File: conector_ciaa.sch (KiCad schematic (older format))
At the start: 2 parts

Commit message: Primer version
Esquematico completo, faltan notas del revisor.
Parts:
- removed J? (x2): CONN_02X20, symbol CONN_02X20
- added XA1: Conn_Poncho2P_2x_20x2, footprints:Conn_Poncho_Completo, symbol Conn_Poncho2P_2x_20x2
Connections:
- net labels added: +3.3V, +5V, ADC_1, GND, GPIO_0, GPIO_1, GPIO_2, GPIO_3, SPI_MISO, SPI_SCK
- wire segments 0 -> 36
- no-connect marks 0 -> 50

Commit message: Primer revision
Se agregar correcciones del revisor. Se modifica entrada termocupla.
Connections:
- net GNDA: now reaches XA1.10 (GNDA)
- no-connect marks 50 -> 49
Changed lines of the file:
@@
 EESchema Schematic File Version 2
-LIBS:tempRalayPoncho-rescue
-LIBS:power
-LIBS:device
-LIBS:transistors
-LIBS:conn
-LIBS:linear
-LIBS:regul
-LIBS:74xx
-LIBS:cmos4000
-LIBS:adc-dac
-LIBS:memory
-LIBS:xilinx
-LIBS:microcontrollers
-LIBS:dsp
-LIBS:microchip
-LIBS:analog_switches
-LIBS:motorola
-LIBS:texas
-LIBS:intel
-LIBS:audio
-LIBS:interface
-LIBS:digital-audio
-LIBS:philips
-LIBS:display
-LIBS:cypress
-LIBS:siliconi
-LIBS:opto
-LIBS:atmel
-LIBS:contrib
-LIBS:valves
-LIBS:ej2cese
-LIBS:analog-cache
-LIBS:ciaa-nxp-cache
-LIBS:relay
-LIBS:cmos_ieee
-LIBS:tempRalayPoncho-cache
+LIBS:TempRelay
+LIBS:tempRelayPoncho-cache
 EELAYER 25 0
 EELAYER END
@@
 Connection ~ 4900 4100
 NoConn ~ 4600 2400
-NoConn ~ 4600 2600
 NoConn ~ 4600 2700
 NoConn ~ 4600 2800
@@
 Wire Wire Line
 	6600 3400 6900 3400
-Wire Wire Line
-	6600 3500 6900 3500
-Connection ~ 6600 3400
 Connection ~ 6600 3100
 Wire Wire Line
 	6600 4000 6900 4000
-Connection ~ 6600 3500
 Wire Wire Line
 	6600 4100 6900 4100
-Connection ~ 6600 4000
 Wire Wire Line
 	6600 4000 6600 4400
@@
 NoConn ~ 8100 4100
 $Comp
-L GND #PWR01
+L GND #PWR3
 U 1 1 594EB190
 P 4900 4400
-F 0 "#PWR01" H 4900 4150 50  0001 C CNN
+F 0 "#PWR3" H 4900 4150 50  0001 C CNN
 F 1 "GND" H 4900 4250 50  0000 C CNN
 F 2 "" H 4900 4400 50  0001 C CNN
@@
 $EndComp
 $Comp
-L GND #PWR02
+L GND #PWR5
 U 1 1 594EB307
 P 6600 4400
-F 0 "#PWR02" H 6600 4150 50  0001 C CNN
+F 0 "#PWR5" H 6600 4150 50  0001 C CNN
 F 1 "GND" H 6600 4250 50  0000 C CNN
 F 2 "" H 6600 4400 50  0001 C CNN
@@
 $EndComp
 $Comp
-L GND #PWR03
+L GND #PWR4
 U 1 1 594EB35A
 P 6200 2600
-F 0 "#PWR03" H 6200 2350 50  0001 C CNN
+F 0 "#PWR4" H 6200 2350 50  0001 C CNN
 F 1 "GND" H 6200 2450 50  0000 C CNN
 F 2 "" H 6200 2600 50  0001 C CNN
@@
 P 3100 2000
 AR Path="/594EB36B" Ref="#PWR5"  Part="1"
-AR Path="/59498167/594EB36B" Ref="#PWR04"  Part="1"
-F 0 "#PWR04" H 3100 1850 50  0001 C CNN
+AR Path="/59498167/594EB36B" Ref="#PWR1"  Part="1"
+F 0 "#PWR1" H 3100 1850 50  0001 C CNN
 F 1 "+3.3V" H 3100 2140 50  0000 C CNN
 F 2 "" H 3100 2000 50  0001 C CNN
@@
 $EndComp
 $Comp
-L +5V #PWR05
+L +5V #PWR2
 U 1 1 594EB38C
 P 4900 2000
-F 0 "#PWR05" H 4900 1850 50  0001 C CNN
+F 0 "#PWR2" H 4900 1850 50  0001 C CNN
 F 1 "+5V" H 4900 2140 50  0000 C CNN
 F 2 "" H 4900 2000 50  0001 C CNN
@@
 NoConn ~ 4600 2500
 $Comp
-L PWR_FLAG #FLG06
+L PWR_FLAG #FLG1
 U 1 1 594EBA4F
 P 5300 2300
-F 0 "#FLG06" H 5300 2375 50  0001 C CNN
+F 0 "#FLG1" H 5300 2375 50  0001 C CNN
 F 1 "PWR_FLAG" H 5300 2450 50  0000 C CNN
 F 2 "" H 5300 2300 50  0001 C CNN
@@
 NoConn ~ 8100 2200
 NoConn ~ 6900 2200
+Wire Wire Line
+	6600 3500 6900 3500
+Connection ~ 6600 3400
+Wire Wire Line
+	4600 2600 5300 2600
+Text HLabel 5300 2600 2    60   UnSpc ~ 0
+GNDA
 $EndSCHEMATC

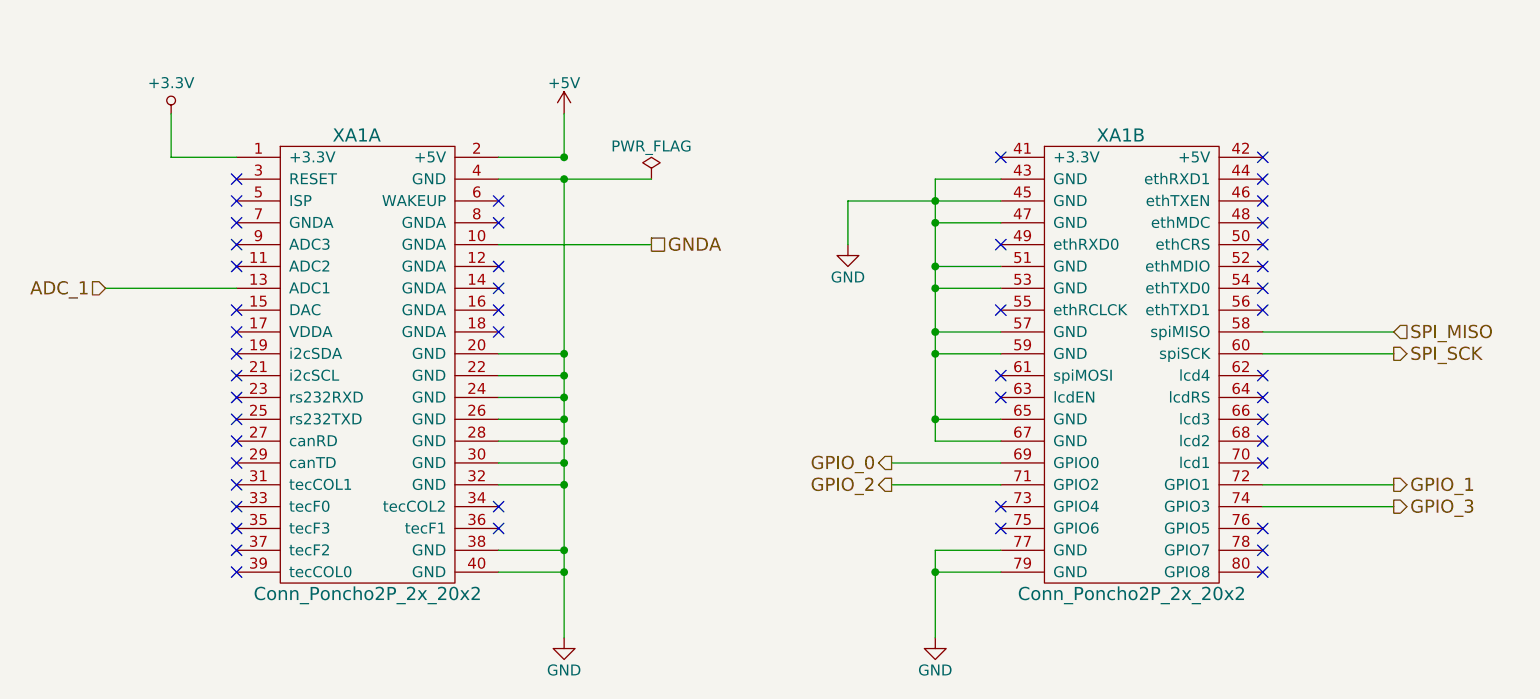
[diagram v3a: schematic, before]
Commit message: Primer version del PCB
Se agregan modificaciones segun primer correccion. Se carga primer version  del PCB.
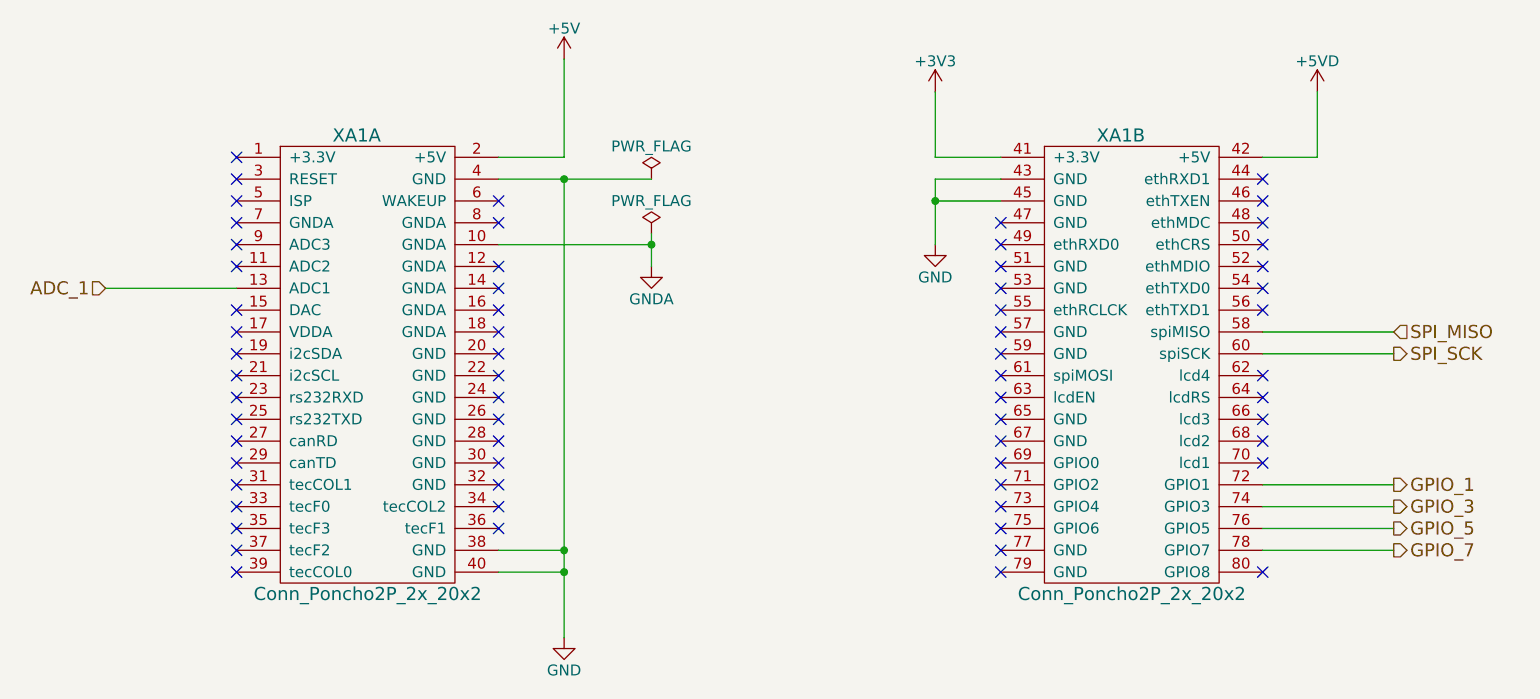
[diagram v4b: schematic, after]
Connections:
- net GND: no longer XA1.20 (GND), XA1.22 (GND), XA1.24 (GND), XA1.26 (GND), XA1.28 (GND), XA1.30 (GND), XA1.32 (GND), XA1.47 (GND), XA1.51 (GND), XA1.53 (GND), XA1.57 (GND), XA1.59 (GND), XA1.65 (GND), XA1.67 (GND), XA1.77 (GND), XA1.79 (GND)
- net +3V3: now reaches XA1.41 (+3.3V)
- net +5VD: now reaches XA1.42 (+5V)
- net GPIO_5: now reaches XA1.76 (GPIO5)
- net GPIO_7: now reaches XA1.78 (GPIO7)
- net +3.3V: no longer names the net of XA1.1 (+3.3V)
- net GPIO_0: no longer names the net of XA1.69 (GPIO0)
- net GPIO_2: no longer names the net of XA1.71 (GPIO2)
- no-connect marks 49 -> 64
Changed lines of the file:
@@
 EESchema Schematic File Version 2
 LIBS:TempRelay
+LIBS:power
 LIBS:tempRelayPoncho-cache
 EELAYER 25 0
@@
 $Descr A4 11693 8268
 encoding utf-8
-Sheet 2 4
+Sheet 3 4
 Title "Poncho Edu CIAA - Sensor Temperatura y Salidas digitales"
 Date "2017-06-14"
 Rev "1.0"
-Comp "Autor: Francisco Suarez"
-Comment1 "Revisor:  Mariano Orlante"
-Comment2 "Licencia: 'Docs/Licencia.txt\""
-Comment3 ""
+Comp "CESE - Trabajo final de la materia \"Diseño de Circuitos Impresos\""
+Comment1 "Licencia: 'Docs/Licencia.txt\""
+Comment2 "Revisor:  Mariano Orlante "
+Comment3 "Autor: Francisco Suárez"
 Comment4 ""
 $EndDescr
@@
 	3400 2800 2800 2800
 Wire Wire Line
-	6900 3600 6400 3600
-Wire Wire Line
-	6400 3700 6900 3700
-Wire Wire Line
 	8100 3000 8700 3000
 Wire Wire Line
 	8100 3100 8700 3100
-Wire Wire Line
-	8100 3700 8700 3700
-Wire Wire Line
-	8100 3800 8700 3800
-Text HLabel 6400 3600 0    60   Output ~ 0
-GPIO_0
-Text HLabel 6400 3700 0    60   Output ~ 0
-GPIO_2
 Text HLabel 8700 3700 2    60   Output ~ 0
 GPIO_1
+Text HLabel 8700 3900 2    60   Output ~ 0
+GPIO_5
 Text HLabel 8700 3800 2    60   Output ~ 0
 GPIO_3
+Text HLabel 8700 4000 2    60   Output ~ 0
+GPIO_7
 Text HLabel 8700 3000 2    60   Input ~ 0
 SPI_MISO
@@
 	4900 2300 4900 4400
 Wire Wire Line
-	4900 3100 4600 3100
-Wire Wire Line
-	4900 3200 4600 3200
-Connection ~ 4900 3100
-Wire Wire Line
-	4900 3300 4600 3300
-Connection ~ 4900 3200
-Wire Wire Line
-	4900 3400 4600 3400
-Connection ~ 4900 3300
-Wire Wire Line
-	4900 3500 4600 3500
-Connection ~ 4900 3400
-Wire Wire Line
-	4900 3600 4600 3600
-Connection ~ 4900 3500
-Wire Wire Line
-	4900 3700 4600 3700
-Connection ~ 4900 3600
-Wire Wire Line
 	4900 4000 4600 4000
-Connection ~ 4900 3700
 Wire Wire Line
 	4900 4100 4600 4100
@@
 NoConn ~ 3400 4100
 Wire Wire Line
-	3400 2200 3100 2200
-Wire Wire Line
-	3100 2200 3100 2000
-Wire Wire Line
-	4900 2200 4900 2000
-Wire Wire Line
 	6900 2300 6600 2300
-Wire Wire Line
-	6200 2400 6900 2400
-Wire Wire Line
-	6600 2500 6900 2500
 Connection ~ 6600 2400
-Wire Wire Line
-	6600 2700 6900 2700
-Connection ~ 6600 2500
-Wire Wire Line
-	6600 2800 6900 2800
-Connection ~ 6600 2700
-Wire Wire Line
-	6600 3000 6900 3000
-Connection ~ 6600 2800
-Wire Wire Line
-	6600 3100 6900 3100
-Connection ~ 6600 3000
-Wire Wire Line
-	6600 3400 6900 3400
-Connection ~ 6600 3100
-Wire Wire Line
-	6600 4000 6900 4000
-Wire Wire Line
-	6600 4100 6900 4100
-Wire Wire Line
-	6600 4000 6600 4400
-Connection ~ 6600 4100
-Wire Wire Line
-	6600 2300 6600 3500
-Wire Wire Line
-	6200 2400 6200 2600
 NoConn ~ 6900 2600
 NoConn ~ 6900 2900
@@
 NoConn ~ 8100 2400
 NoConn ~ 8100 2300
-NoConn ~ 8100 3900
-NoConn ~ 8100 4000
 NoConn ~ 8100 4100
 $Comp
-L GND #PWR01
+L GND #PWR07
 U 1 1 594EB190
 P 4900 4400
-F 0 "#PWR01" H 4900 4150 50  0001 C CNN
+F 0 "#PWR07" H 4900 4150 50  0001 C CNN
 F 1 "GND" H 4900 4250 50  0000 C CNN
 F 2 "" H 4900 4400 50  0001 C CNN
@@
 $EndComp
 $Comp
-L GND #PWR02
-U 1 1 594EB307
-P 6600 4400
-F 0 "#PWR02" H 6600 4150 50  0001 C CNN
-F 1 "GND" H 6600 4250 50  0000 C CNN
-F 2 "" H 6600 4400 50  0001 C CNN
-F 3 "" H 6600 4400 50  0001 C CNN
-	1    6600 4400
-	1    0    0    -1
-$EndComp
-$Comp
-L GND #PWR03
+L GND #PWR09
 U 1 1 594EB35A
-P 6200 2600
-F 0 "#PWR03" H 6200 2350 50  0001 C CNN
-F 1 "GND" H 6200 2450 50  0000 C CNN
-F 2 "" H 6200 2600 50  0001 C CNN
-F 3 "" H 6200 2600 50  0001 C CNN
-	1    6200 2600
-	1    0    0    -1
-$EndComp
-$Comp
-L +3.3V-RESCUE-tempRalayPoncho #PWR5
-U 1 1 594EB36B
-P 3100 2000
-AR Path="/594EB36B" Ref="#PWR5"  Part="1"
-AR Path="/59498167/594EB36B" Ref="#PWR04"  Part="1"
-F 0 "#PWR04" H 3100 1850 50  0001 C CNN
-F 1 "+3.3V" H 3100 2140 50  0000 C CNN
-F 2 "" H 3100 2000 50  0001 C CNN
-F 3 "" H 3100 2000 50  0001 C CNN
-	1    3100 2000
-	1    0    0    -1
-$EndComp
-$Comp
-L +5V #PWR05
+P 6600 2600
+F 0 "#PWR09" H 6600 2350 50  0001 C CNN
+F 1 "GND" H 6600 2450 50  0000 C CNN
+F 2 "" H 6600 2600 50  0001 C CNN
+F 3 "" H 6600 2600 50  0001 C CNN
+	1    6600 2600
+	1    0    0    -1
+$EndComp
+$Comp
+L +5V #PWR010
 U 1 1 594EB38C
-P 4900 2000
-F 0 "#PWR05" H 4900 1850 50  0001 C CNN
-F 1 "+5V" H 4900 2140 50  0000 C CNN
-F 2 "" H 4900 2000 50  0001 C CNN
-F 3 "" H 4900 2000 50  0001 C CNN
-	1    4900 2000
+P 4900 1750
+F 0 "#PWR010" H 4900 1600 50  0001 C CNN
+F 1 "+5V" H 4900 1890 50  0000 C CNN
+F 2 "" H 4900 1750 50  0001 C CNN
+F 3 "" H 4900 1750 50  0001 C CNN
+	1    4900 1750
 	1    0    0    -1
 $EndComp
 NoConn ~ 4600 2500
 $Comp
-L PWR_FLAG #FLG06
+L PWR_FLAG #FLG011
 U 1 1 594EBA4F
 P 5300 2300
-F 0 "#FLG06" H 5300 2375 50  0001 C CNN
+F 0 "#FLG011" H 5300 2375 50  0001 C CNN
 F 1 "PWR_FLAG" H 5300 2450 50  0000 C CNN
 F 2 "" H 5300 2300 50  0001 C CNN
@@
 Connection ~ 4900 2300
 NoConn ~ 3400 2500
-Connection ~ 4900 2200
-Wire Wire Line
-	4600 2200 4900 2200
-NoConn ~ 8100 2200
-NoConn ~ 6900 2200
-Wire Wire Line
-	6600 3500 6900 3500
-Connection ~ 6600 3400
 Wire Wire Line
 	4600 2600 5300 2600
-Text HLabel 5300 2600 2    60   UnSpc ~ 0
-GNDA
+$Comp
+L GNDA #PWR012
+U 1 1 5962BA55
+P 5300 2700
+F 0 "#PWR012" H 5300 2450 50  0001 C CNN
+F 1 "GNDA" H 5300 2550 50  0000 C CNN
+F 2 "" H 5300 2700 50  0001 C CNN
+F 3 "" H 5300 2700 50  0001 C CNN
+	1    5300 2700
+	1    0    0    -1
+$EndComp
+Wire Wire Line
+	5300 2550 5300 2700
+$Comp
+L PWR_FLAG #FLG013
+U 1 1 59630D10
+P 5300 2550
+F 0 "#FLG013" H 5300 2625 50  0001 C CNN
+F 1 "PWR_FLAG" H 5300 2700 50  0000 C CNN
+F 2 "" H 5300 2550 50  0001 C CNN
+F 3 "" H 5300 2550 50  0001 C CNN
+	1    5300 2550
+	1    0    0    -1
+$EndComp
+Connection ~ 5300 2600
+NoConn ~ 6900 3600
+NoConn ~ 6900 3700
+Wire Wire Line
+	8700 3700 8100 3700
+Wire Wire Line
+	8100 3800 8700 3800
+Wire Wire Line
+	8700 3900 8100 3900
+Wire Wire Line
+	8100 4000 8700 4000
+Wire Wire Line
+	4900 1750 4900 2200
+Wire Wire Line
+	4900 2200 4600 2200
+Wire Wire Line
+	8350 1900 8350 2200
+Wire Wire Line
+	8350 2200 8100 2200
+$Comp
+L +5VD #PWR014
+U 1 1 596C77DA
+P 8350 1900
+F 0 "#PWR014" H 8350 1750 50  0001 C CNN
+F 1 "+5VD" H 8350 2040 50  0000 C CNN
+F 2 "" H 8350 1900 50  0001 C CNN
+F 3 "" H 8350 1900 50  0001 C CNN
+	1    8350 1900
+	1    0    0    -1
+$EndComp
+Wire Wire Line
+	6900 2200 6600 2200
+Wire Wire Line
+	6600 2200 6600 1900
+$Comp
+L +3V3 #PWR015
+U 1 1 596C783A
+P 6600 1900
+F 0 "#PWR015" H 6600 1750 50  0001 C CNN
+F 1 "+3V3" H 6600 2040 50  0000 C CNN
+F 2 "" H 6600 1900 50  0001 C CNN
+F 3 "" H 6600 1900 50  0001 C CNN
+	1    6600 1900
+	1    0    0    -1
+$EndComp
+NoConn ~ 3400 2200
+NoConn ~ 4600 3100
+NoConn ~ 4600 3200
+NoConn ~ 4600 3300
+NoConn ~ 4600 3400
+NoConn ~ 4600 3500
+NoConn ~ 4600 3600
+NoConn ~ 4600 3700
+Wire Wire Line
+	6600 2300 6600 2600
+NoConn ~ 6900 2700
+NoConn ~ 6900 2500
+NoConn ~ 6900 2800
+NoConn ~ 6900 3000
+NoConn ~ 6900 3100
+NoConn ~ 6900 3400
+NoConn ~ 6900 3500
+NoConn ~ 6900 4000
+NoConn ~ 6900 4100
+Wire Wire Line
+	6900 2400 6600 2400
 $EndSCHEMATC
